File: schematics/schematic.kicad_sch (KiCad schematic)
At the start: 9 parts, among them J1 USB_A, SW1 SW_DIP_x01, SW2 OKY3431-4, U1 Pico, U2 Pico W

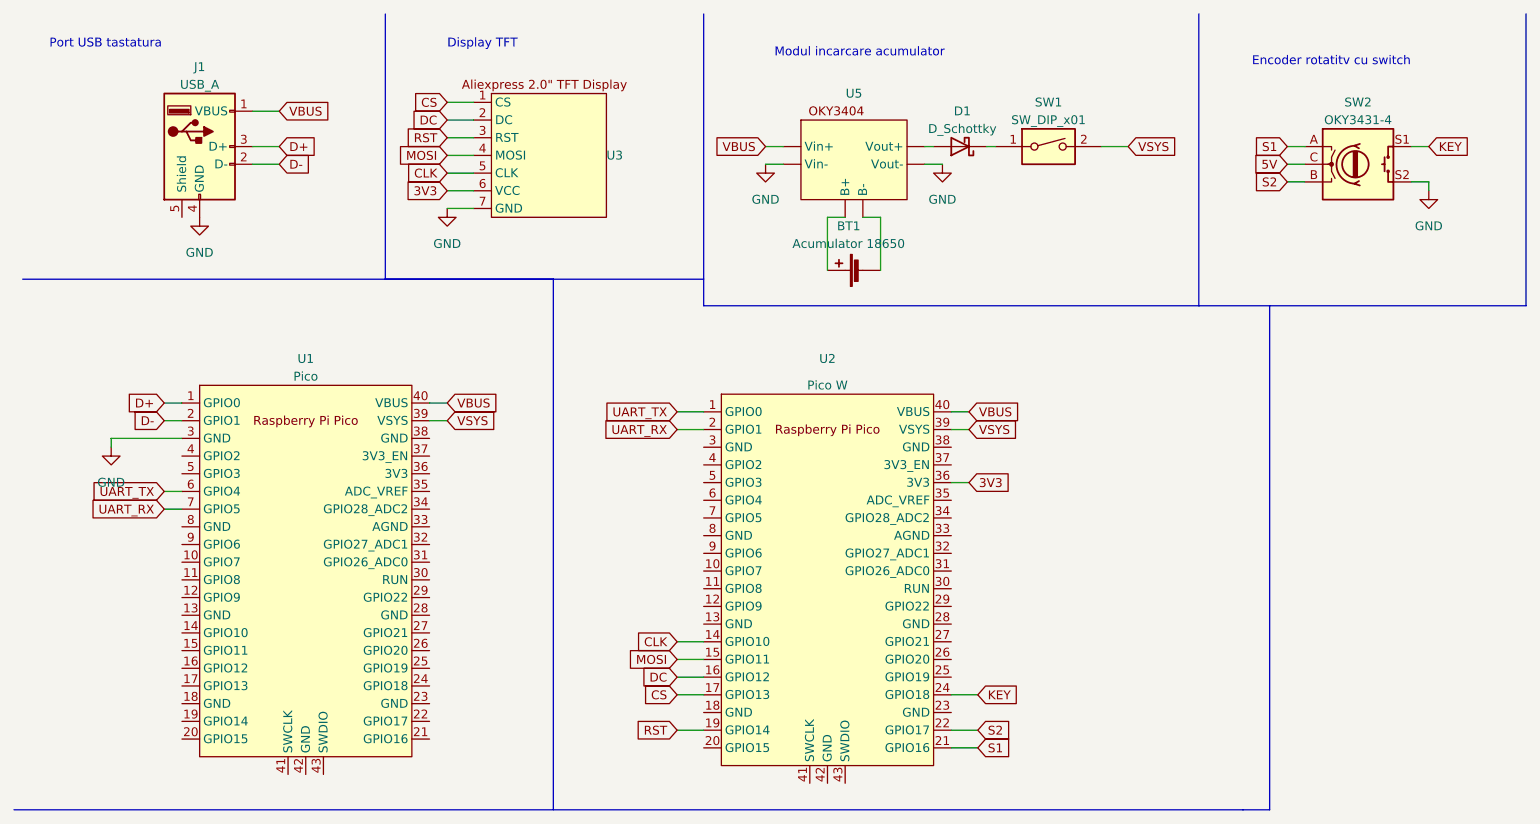
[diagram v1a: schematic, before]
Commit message: Replace diode with p-mosfet
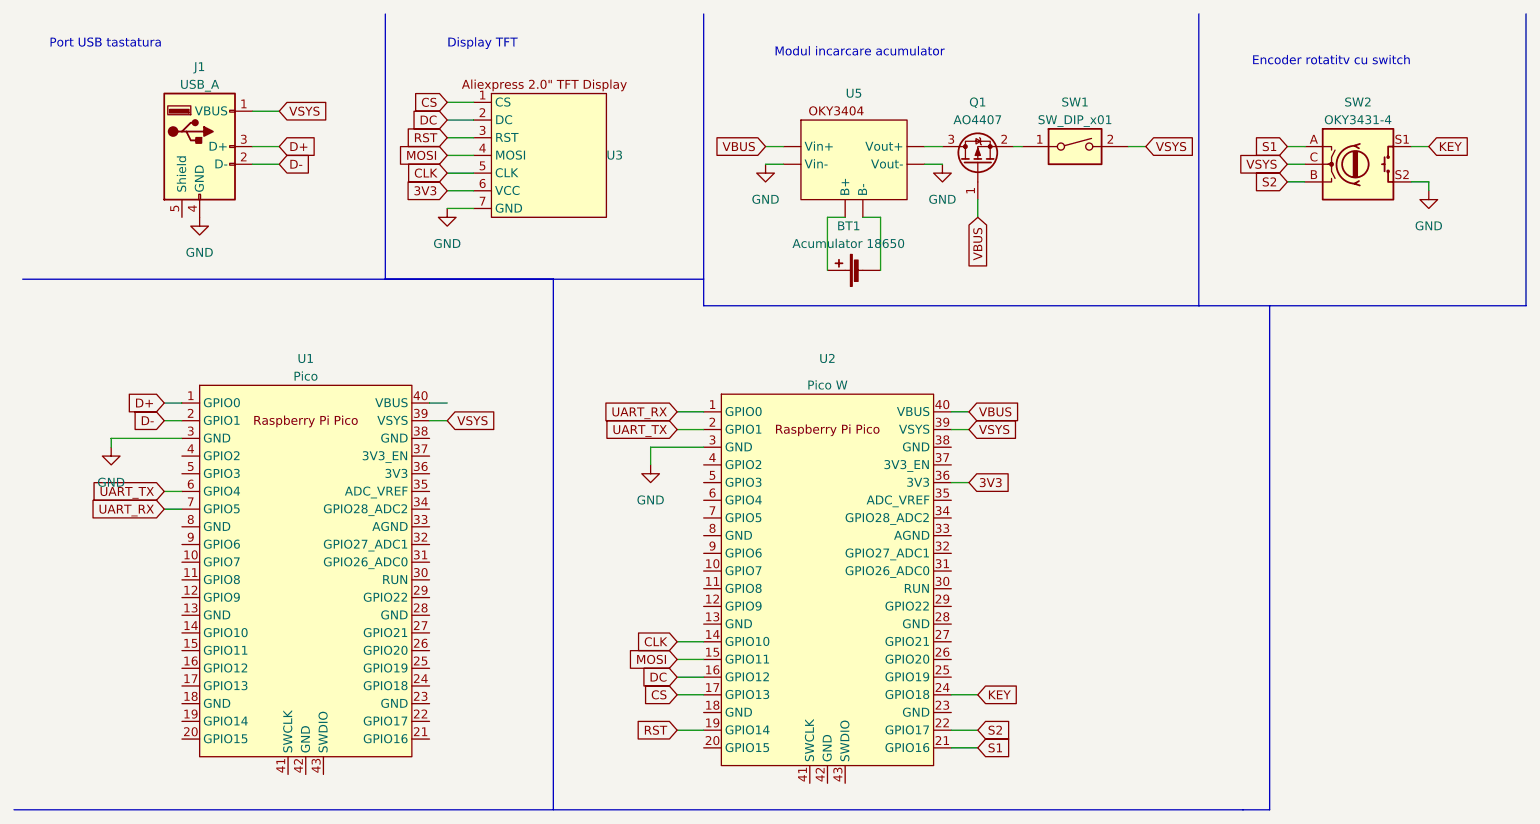
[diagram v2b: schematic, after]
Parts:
- removed D1: D_Schottky, symbol Device:D_Schottky
- added Q1: AO4407, symbol Device:Q_PMOS_GSD
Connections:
- net 5V is gone; now on net VSYS: SW2.C
- net GND: now also U2.3 (GND)
- net UART_RX: now also U2.1 (GPIO0); no longer U2.2 (GPIO1)
- net UART_TX: now also U2.2 (GPIO1); no longer U2.1 (GPIO0)
- net VBUS: now also Q1.1 (G); no longer J1.1 (VBUS), U1.40 (VBUS)
- net VSYS: now also J1.1 (VBUS)
- net at SW1.1: now also Q1.2 (S)
- new net: Q1.3 (D), U5. (Vout-)
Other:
- moved on the sheet: SW1
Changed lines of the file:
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@@
+    (stroke (width 0) (type default))
+  )
+  (wire (pts (xy 101.6 73.66) (xy 101.6 76.2))
     (stroke (width 0) (type default))
   )
@@
     (stroke (width 0) (type default))
   )
+  (wire (pts (xy 153.67 30.48) (xy 154.94 30.48))
+    (stroke (width 0) (type default))
+  )
+  (wire (pts (xy 109.22 73.66) (xy 101.6 73.66))
+    (stroke (width 0) (type default))
+  )
   (wire (pts (xy 44.45 25.4) (xy 48.26 25.4))
     (stroke (width 0) (type default))
@@
     (stroke (width 0) (type default))
   )
-  (wire (pts (xy 149.86 30.48) (xy 151.13 30.48))
-    (stroke (width 0) (type default))
-  )
   (wire (pts (xy 72.39 34.29) (xy 76.2 34.29))
     (stroke (width 0) (type default))
@@
     (stroke (width 0) (type default))
   )
-  (wire (pts (xy 166.37 30.48) (xy 170.18 30.48))
+  (wire (pts (xy 170.18 30.48) (xy 172.72 30.48))
     (stroke (width 0) (type default))
   )
@@
     (stroke (width 0) (type default))
   )
+  (wire (pts (xy 148.59 38.1) (xy 148.59 40.64))
+    (stroke (width 0) (type default))
+  )
   (wire (pts (xy 72.39 31.75) (xy 76.2 31.75))
     (stroke (width 0) (type default))
   )
-  (wire (pts (xy 140.97 30.48) (xy 142.24 30.48))
+  (wire (pts (xy 140.97 30.48) (xy 143.51 30.48))
     (stroke (width 0) (type default))
   )
@@
     )
   )
-  (global_label "UART_TX" (shape input) (at 105.41 68.58 180) (fields_autoplaced)
-    (effects (font (size 1.27 1.27)) (justify right))
-    (property "Intersheetrefs" "${INTERSHEET_REFS}" (at 94.7028 68.58 0)
+  (global_label "UART_RX" (shape input) (at 105.41 68.58 180) (fields_autoplaced)
+    (effects (font (size 1.27 1.27)) (justify right))
+    (property "Intersheetrefs" "${INTERSHEET_REFS}" (at 94.4004 68.58 0)
       (effects (font (size 1.27 1.27)) (justify right) hide)
     )
@@
     )
   )
-  (global_label "UART_RX" (shape input) (at 105.41 71.12 180) (fields_autoplaced)
-    (effects (font (size 1.27 1.27)) (justify right))
-    (property "Intersheetrefs" "${INTERSHEET_REFS}" (at 94.4004 71.12 0)
+  (global_label "UART_TX" (shape input) (at 105.41 71.12 180) (fields_autoplaced)
+    (effects (font (size 1.27 1.27)) (justify right))
+    (property "Intersheetrefs" "${INTERSHEET_REFS}" (at 94.7028 71.12 0)
       (effects (font (size 1.27 1.27)) (justify right) hide)
     )
@@
     )
   )
-  (global_label "VBUS" (shape input) (at 48.26 25.4 0) (fields_autoplaced)
-    (effects (font (size 1.27 1.27)) (justify left))
-    (property "Intersheetrefs" "${INTERSHEET_REFS}" (at 56.0644 25.4 0)
+  (global_label "VSYS" (shape input) (at 48.26 25.4 0) (fields_autoplaced)
+    (effects (font (size 1.27 1.27)) (justify left))
+    (property "Intersheetrefs" "${INTERSHEET_REFS}" (at 55.762 25.4 0)
       (effects (font (size 1.27 1.27)) (justify left) hide)
     )
@@
     )
   )
-  (global_label "VSYS" (shape input) (at 170.18 30.48 0) (fields_autoplaced)
-    (effects (font (size 1.27 1.27)) (justify left))
-    (property "Intersheetrefs" "${INTERSHEET_REFS}" (at 177.682 30.48 0)
+  (global_label "VSYS" (shape input) (at 172.72 30.48 0) (fields_autoplaced)
+    (effects (font (size 1.27 1.27)) (justify left))
+    (property "Intersheetrefs" "${INTERSHEET_REFS}" (at 180.222 30.48 0)
       (effects (font (size 1.27 1.27)) (justify left) hide)
     )
@@
     )
   )
+  (global_label "VBUS" (shape input) (at 148.59 40.64 270) (fields_autoplaced)
+    (effects (font (size 1.27 1.27)) (justify right))
+    (property "Intersheetrefs" "${INTERSHEET_REFS}" (at 148.59 48.4444 90)
+      (effects (font (size 1.27 1.27)) (justify right) hide)
+    )
+  )
   (global_label "DC" (shape input) (at 72.39 26.67 180) (fields_autoplaced)
     (effects (font (size 1.27 1.27)) (justify right))
@@
     )
   )
-  (global_label "VBUS" (shape input) (at 72.39 67.31 0) (fields_autoplaced)
-    (effects (font (size 1.27 1.27)) (justify left))
-    (property "Intersheetrefs" "${INTERSHEET_REFS}" (at 80.1944 67.31 0)
-      (effects (font (size 1.27 1.27)) (justify left) hide)
-    )
-  )
-  (global_label "5V" (shape input) (at 193.04 33.02 180) (fields_autoplaced)
-    (effects (font (size 1.27 1.27)) (justify right))
-    (property "Intersheetrefs" "${INTERSHEET_REFS}" (at 187.8361 33.02 0)
+  (global_label "VSYS" (shape input) (at 193.04 33.02 180) (fields_autoplaced)
+    (effects (font (size 1.27 1.27)) (justify right))
+    (property "Intersheetrefs" "${INTERSHEET_REFS}" (at 185.538 33.02 0)
       (effects (font (size 1.27 1.27)) (justify right) hide)
     )
@@
     )
   )
-  (symbol (lib_id "Switch:SW_DIP_x01") (at 158.75 30.48 0) (unit 1)
-    (in_bom yes) (on_board yes) (dnp no) (fields_autoplaced)
-    (property "Reference" "SW1" (at 158.75 24.13 0)
-      (effects (font (size 1.27 1.27)))
-    )
-    (property "Value" "SW_DIP_x01" (at 158.75 26.67 0)
-      (effects (font (size 1.27 1.27)))
-    )
-    (property "Footprint" "" (at 158.75 30.48 0)
-      (effects (font (size 1.27 1.27)) hide)
-    )
-    (property "Datasheet" "~" (at 158.75 30.48 0)
+  (symbol (lib_id "Switch:SW_DIP_x01") (at 162.56 30.48 0) (unit 1)
+    (in_bom yes) (on_board yes) (dnp no) (fields_autoplaced)
+    (property "Reference" "SW1" (at 162.56 24.13 0)
+      (effects (font (size 1.27 1.27)))
+    )
+    (property "Value" "SW_DIP_x01" (at 162.56 26.67 0)
+      (effects (font (size 1.27 1.27)))
+    )
+    (property "Footprint" "" (at 162.56 30.48 0)
+      (effects (font (size 1.27 1.27)) hide)
+    )
+    (property "Datasheet" "~" (at 162.56 30.48 0)
       (effects (font (size 1.27 1.27)) hide)
     )
@@
         (path "/1b147fc8-d3e6-476b-8793-6266a12930f3"
           (reference "BT1") (unit 1)
-        )
-      )
-    )
-  )
-  (symbol (lib_id "Device:D_Schottky") (at 146.05 30.48 180) (unit 1)
-    (in_bom yes) (on_board yes) (dnp no) (fields_autoplaced)
-    (property "Reference" "D1" (at 146.3675 25.4 0)
-      (effects (font (size 1.27 1.27)))
-    )
-    (property "Value" "D_Schottky" (at 146.3675 27.94 0)
-      (effects (font (size 1.27 1.27)))
-    )
-    (property "Footprint" "" (at 146.05 30.48 0)
-      (effects (font (size 1.27 1.27)) hide)
-    )
-    (property "Datasheet" "~" (at 146.05 30.48 0)
-      (effects (font (size 1.27 1.27)) hide)
-    )
-    (pin "1")
-    (pin "2")
-    (instances
-      (project "schematic"
-        (path "/1b147fc8-d3e6-476b-8793-6266a12930f3"
-          (reference "D1") (unit 1)
         )
       )
@@
         )
       )
+    )
+  )
+  (symbol (lib_id "Device:Q_PMOS_GSD") (at 148.59 33.02 90) (unit 1)
+    (in_bom yes) (on_board yes) (dnp no) (fields_autoplaced)
+    (property "Reference" "Q1" (at 148.59 24.13 90)
+      (effects (font (size 1.27 1.27)))
+    )
+    (property "Value" "AO4407" (at 148.59 26.67 90)
+      (effects (font (size 1.27 1.27)))
+    )
+    (property "Footprint" "" (at 146.05 27.94 0)
+      (effects (font (size 1.27 1.27)) hide)
+    )
+    (property "Datasheet" "~" (at 148.59 33.02 0)
+      (effects (font (size 1.27 1.27)) hide)
+    )
+    (pin "1")
+    (pin "2")
+    (pin "3")
+    (instances
+      (project "schematic"
+        (path "/1b147fc8-d3e6-476b-8793-6266a12930f3"
+          (reference "Q1") (unit 1)
+        )
+      )
+    )
+  )
+  (symbol (lib_id "power:GND") (at 101.6 76.2 0) (unit 1)
+    (in_bom yes) (on_board yes) (dnp no) (fields_autoplaced)
+    (property "Reference" "#PWR04" (at 101.6 82.55 0)
+      (effects (font (size 1.27 1.27)) hide)
+    )
+    (property "Value" "GND" (at 101.6 81.28 0)
+      (effects (font (size 1.27 1.27)))
+    )
+    (property "Footprint" "" (at 101.6 76.2 0)
+      (effects (font (size 1.27 1.27)) hide)
+    )
+    (property "Datasheet" "" (at 101.6 76.2 0)
+      (effects (font (size 1.27 1.27)) hide)
+    )
+    (pin "1")
+    (instances
+      (project "schematic"
+        (path "/1b147fc8-d3e6-476b-8793-6266a12930f3"
+          (reference "#PWR04") (unit 1)
+        )
+      )
